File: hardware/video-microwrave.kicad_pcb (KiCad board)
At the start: 2 copper layers, 104.8 x 101.6 mm, 78 parts, among them J501 PJ301M-12, J502 PJ301M-12, J503 PJ301M-12, J504 PJ301M-12, J505 PJ301M-12, J506 PJ301M-12, J507 PJ301M-12, J508 PJ301M-12, P101 CONN_01X09, P102 CONN_01X09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

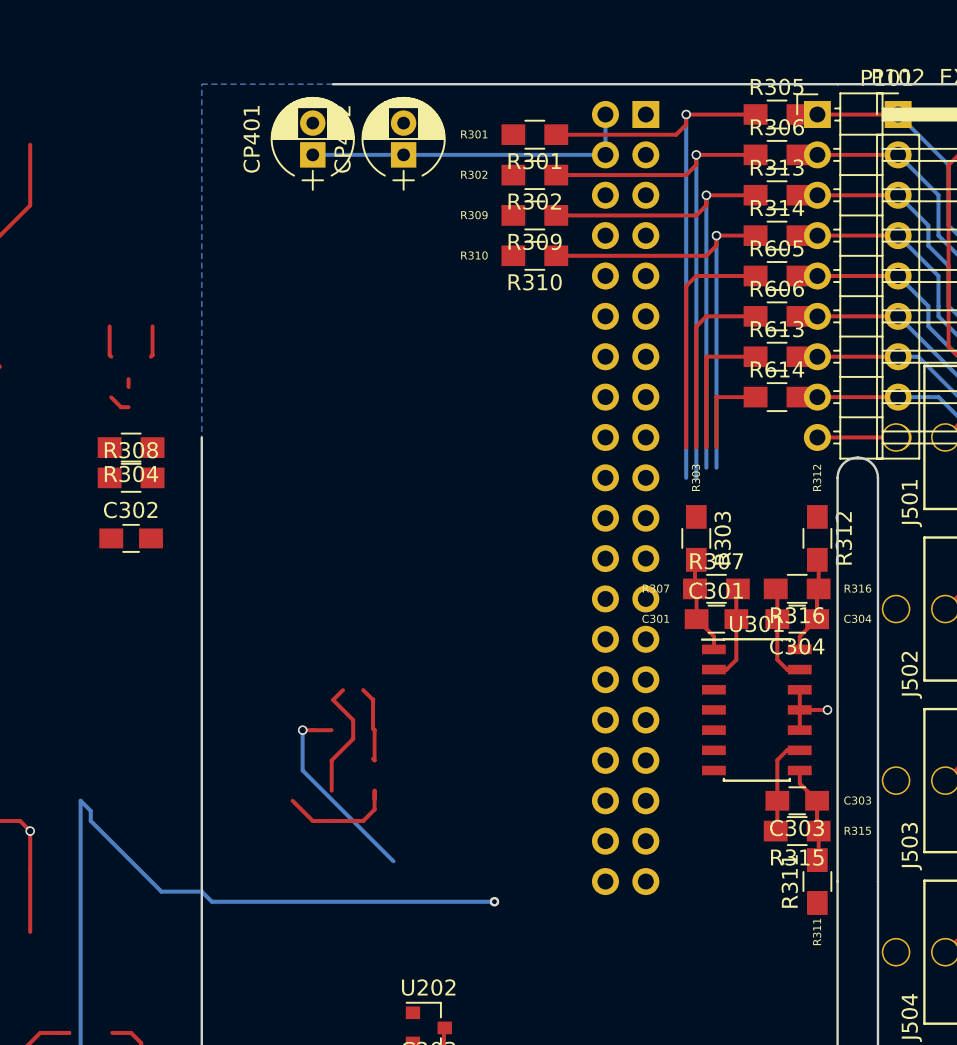
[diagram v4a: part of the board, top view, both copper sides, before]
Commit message: planned 5V and 3.3V lines
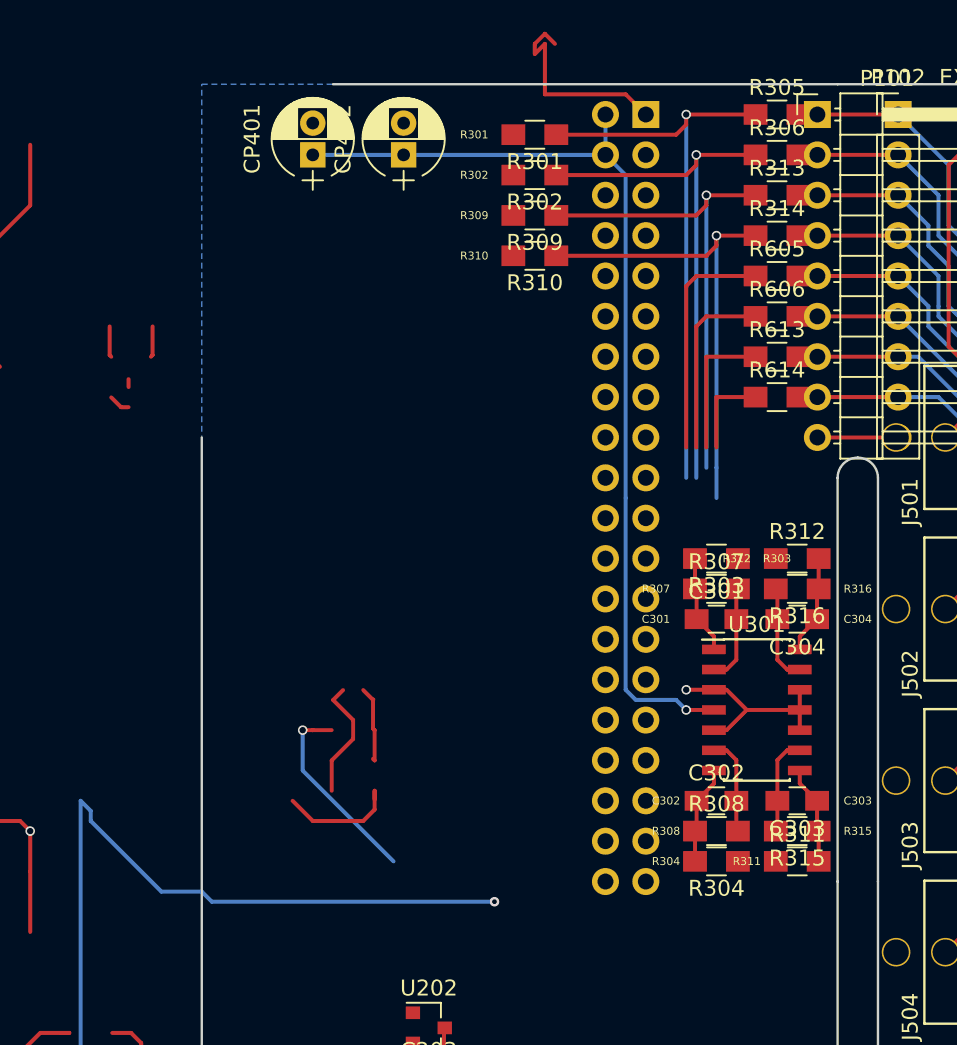
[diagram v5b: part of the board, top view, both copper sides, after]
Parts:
- moved R304 45.1 mm to (144.8, 87.0)
- moved R308 43.0 mm to (144.8, 85.1)
- moved C302 40.4 mm to (144.8, 83.2)
- moved R303 1.80 mm to (144.8, 67.9), turned to 180 degrees
- moved R311 1.80 mm to (149.9, 87.0), turned to 0 degrees
- moved R312 1.80 mm to (149.9, 67.9), turned to 0 degrees
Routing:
- net +5V: track 100.0 -> 140.3 mm, vias 7 -> 8
- net +3V3: track 21.8 -> 35.0 mm
- net Earth: track 159.9 -> 168.4 mm
- net Net-(C302-Pad1): track 0.00 -> 6.21 mm
- net Net-(C302-Pad2): track 33.8 -> 39.9 mm
- net Net-(C304-Pad2): track 34.3 -> 36.2 mm

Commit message: rotated first op amp & shofted 40-pin connector to match 3d model
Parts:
- C201: value 1uF -> 100nF
- P201: value CONN_02X05 -> CONN_02X08
- U201: value MP1469 -> LM1117-3.3
- moved R609 118.5 mm to (133.3, 56.5)
- moved R610 113.7 mm to (133.3, 59.1), turned to 180 degrees
- moved R601 107.8 mm to (133.3, 51.4), turned to 180 degrees
- moved R602 105.5 mm to (133.3, 54.0)
- moved U101 7.62 mm to (140.3, 47.6)
- moved C301 5.08 mm to (149.9, 71.8), turned to 180 degrees
- moved C302 5.08 mm to (149.9, 83.2), turned to 180 degrees
- moved C303 5.08 mm to (144.8, 83.2), turned to 0 degrees
- moved C304 5.08 mm to (144.8, 71.8), turned to 0 degrees
- moved R303 5.08 mm to (149.9, 67.9), turned to 0 degrees
- moved R304 5.08 mm to (149.9, 87.0), turned to 0 degrees
- moved R307 5.08 mm to (149.9, 69.8), turned to 180 degrees
- moved R308 5.08 mm to (149.9, 85.1), turned to 180 degrees
- moved R311 5.08 mm to (144.8, 87.0), turned to 180 degrees
- moved R312 5.08 mm to (144.8, 67.9), turned to 180 degrees
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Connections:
- C201 pad 1: Net-(C201-Pad1) -> Earth
- C201 pad 2: Net-(C201-Pad2) -> +5V
- C244 pad 1: +5V -> VEE
- CP202 pad 1: VCC -> +5V
- L202 pad 1: VCC -> +5V
- L202 pad 2: /power/+12 -> (no net)
- L203 pad 1: +5V -> Net-(L203-Pad1)
- L203 pad 2: Net-(C201-Pad1) -> +5V
- P201 pad 10: /power/+12 -> (no net)
- P201 pad 9: /power/+12 -> (no net)
- R201 pad 1: Net-(R201-Pad1) -> (no net)
- R201 pad 2: VCC -> (no net)
- R203 pad 2: Net-(R203-Pad2) -> (no net)
- U201 pad 1: VCC -> Earth
- U201 pad 2: Earth -> +3V3
- U201 pad 3: Net-(C201-Pad1) -> Net-(L203-Pad1)
- U201 pad 4: Net-(C201-Pad2) -> +3V3
- U201 pad 5: Net-(R201-Pad1) -> (no net)
- U201 pad 6: Net-(R203-Pad2) -> (no net)
- U301 pad 1: Net-(C301-Pad1) -> Net-(C304-Pad1)
- U301 pad 13: Net-(C304-Pad2) -> Net-(C301-Pad2)
- U301 pad 14: Net-(C304-Pad1) -> Net-(C301-Pad1)
- U301 pad 2: Net-(C301-Pad2) -> Net-(C304-Pad2)
- U301 pad 6: Net-(C302-Pad2) -> Net-(C303-Pad2)
- U301 pad 7: Net-(C302-Pad1) -> Net-(C303-Pad1)
- U301 pad 8: Net-(C303-Pad1) -> Net-(C302-Pad1)
- U301 pad 9: Net-(C303-Pad2) -> Net-(C302-Pad2)
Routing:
- net (no net): track 502.8 -> 652.5 mm
- net +5V: track 140.3 -> 69.0 mm, vias 8 -> 7
- net /power/+12: track 66.9 -> 0.00 mm
- net Net-(C601-Pad2): track 24.1 -> 57.2 mm
- net VEE: track 13.0 -> 44.6 mm, vias 0 -> 1
- net Net-(C303-Pad2): track 36.9 -> 60.3 mm, vias 1 -> 2
- net Net-(C302-Pad2): track 39.9 -> 60.8 mm, vias 1 -> 2
- net Net-(C301-Pad2): track 42.6 -> 63.2 mm, vias 1 -> 2
- net VCC: track 17.9 -> 0.00 mm
- net Net-(R203-Pad2): track 13.1 -> 0.00 mm
- net Net-(C304-Pad2): track 36.2 -> 48.9 mm, vias 1 -> 2
- net Net-(R201-Pad1): track 12.1 -> 0.00 mm
- net Net-(C201-Pad1): track 10.8 -> 0.00 mm
- net +3V3: track 35.0 -> 24.5 mm
- net Net-(C201-Pad2): track 1.65 -> 0.00 mm
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
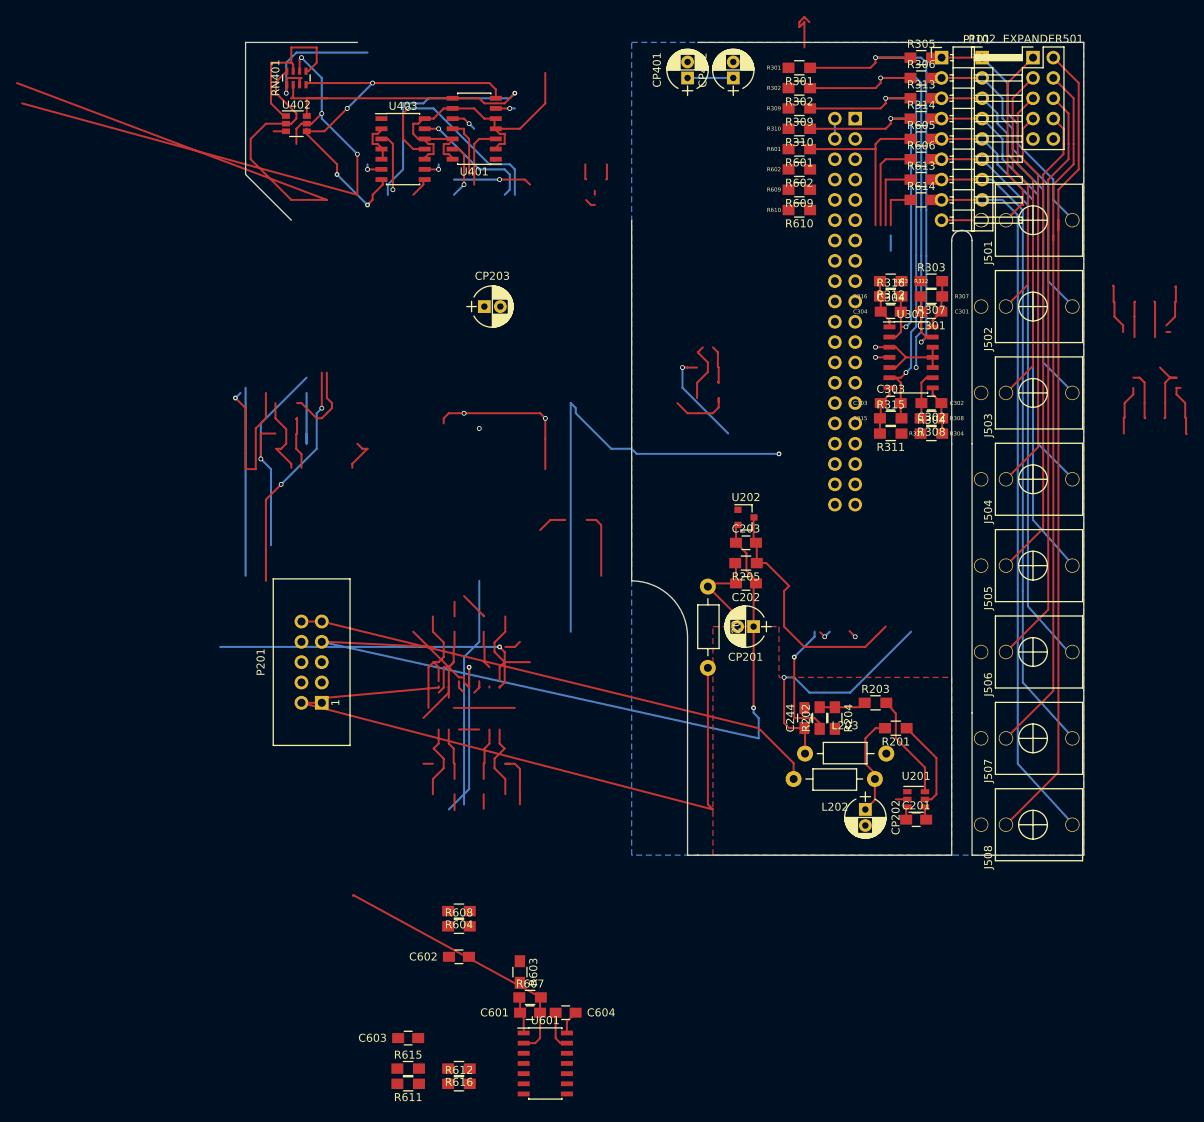
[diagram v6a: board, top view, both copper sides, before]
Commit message: Updates for KiCAD5. Reverted schematic to MCP3008
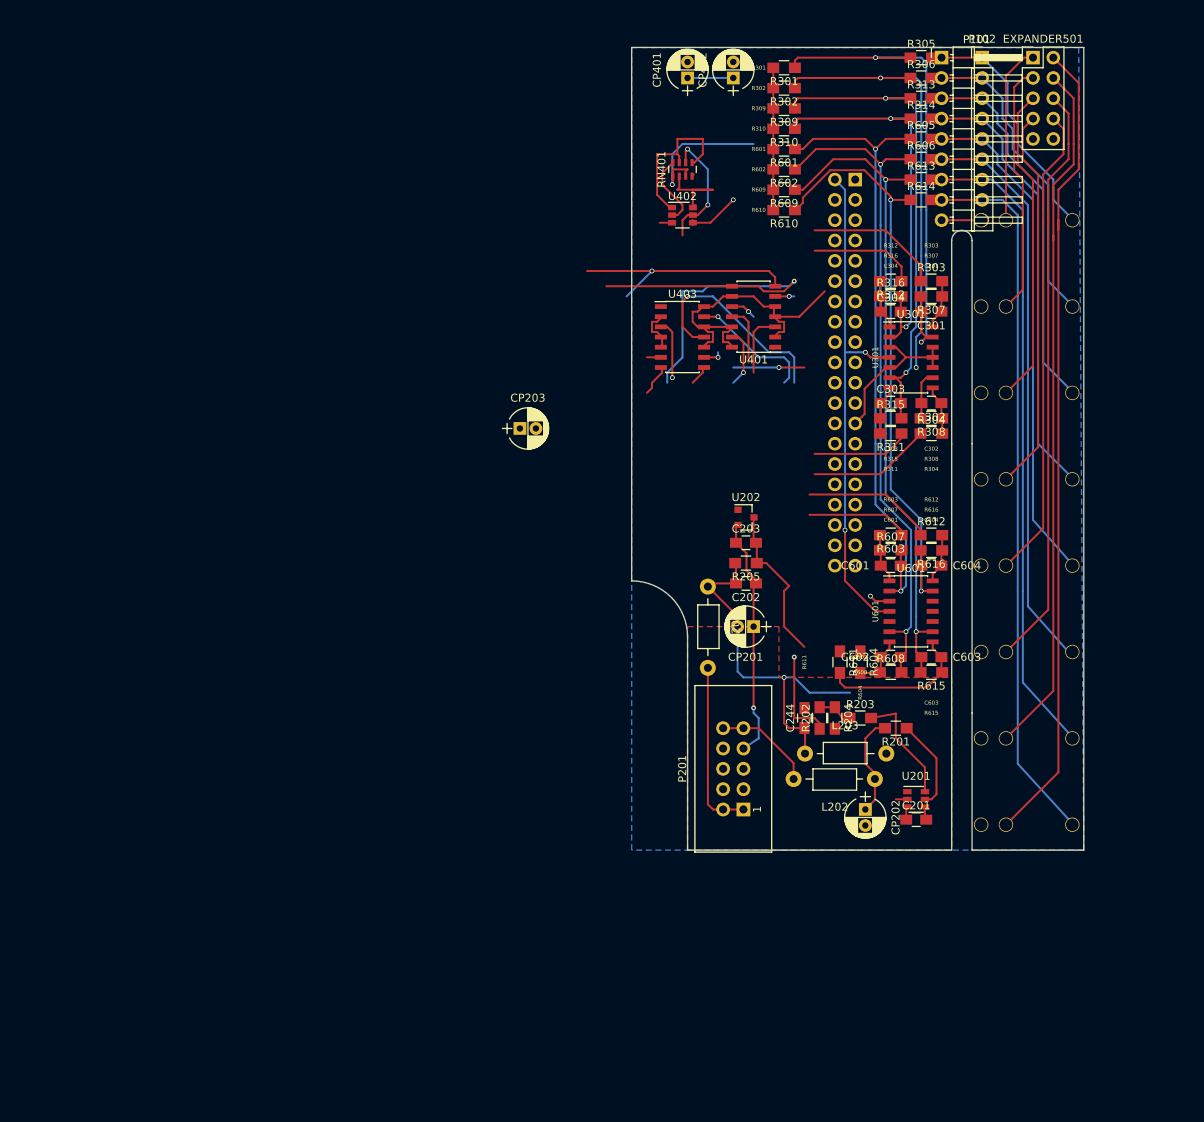
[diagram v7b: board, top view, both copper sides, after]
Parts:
- J501, J502, J503, J504, J505, J506, J507, J508: moved to B.Cu
- moved R612 90.5 mm to (149.9, 99.7)
- moved R616 87.7 mm to (149.9, 101.6)
- moved R615 82.0 mm to (149.9, 116.8), turned to 180 degrees
- moved C603 80.9 mm to (149.9, 114.9), turned to 180 degrees
- moved R611 75.4 mm to (138.4, 115.6), turned to 270 degrees
- moved U601 72.7 mm to (147.3, 109.2)
- moved C604 72.2 mm to (149.9, 103.5)
- moved C601 71.8 mm to (144.8, 103.5)
- moved R607 71.8 mm to (144.8, 101.6)
- moved R603 71.6 mm to (144.8, 99.7), turned to 180 degrees
- moved C602 65.7 mm to (144.8, 114.9)
- moved R608 62.6 mm to (144.8, 116.8)
- moved R604 59.0 mm to (141.0, 115.6), turned to 270 degrees
- moved P201 54.4 mm to (126.4, 134.0)
- moved RN401 49.6 mm to (118.7, 54.0)
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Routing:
- net (no net): track 652.5 -> 48.0 mm, vias 14 -> 1
- net Net-(C603-Pad2): track 8.81 -> 82.7 mm, vias 0 -> 2
- net Net-(C602-Pad2): track 11.6 -> 84.3 mm, vias 0 -> 2
- net /power/-12: track 87.8 -> 21.8 mm
- net Net-(C604-Pad2): track 10.5 -> 75.7 mm, vias 0 -> 2
- net Earth: track 168.4 -> 107.6 mm
- net /I2C_data: track 69.9 -> 9.10 mm
- net +5V: track 69.0 -> 125.2 mm
- net /I2C_clock: track 71.8 -> 15.7 mm, vias 3 -> 2
- net Net-(C601-Pad2): track 57.2 -> 79.8 mm, vias 0 -> 2
- net Net-(C603-Pad1): track 0.00 -> 19.3 mm
- net /buffered_1: track 0.34 -> 17.4 mm
- net /buffered_8: track 27.0 -> 43.4 mm
- net /buffered_2: track 8.04 -> 23.4 mm
- net /buffered_4: track 7.30 -> 20.8 mm
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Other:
- board size 104.8 x 101.6 mm -> 56.5 x 100.3 mm
